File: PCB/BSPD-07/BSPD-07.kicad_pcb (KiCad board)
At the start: 2 copper layers, 78.7 x 30 mm, 17 parts, among them IC1 LM393LVQDRQ1, IC2 LM393LVQDRQ1, IC3 LM393LVQDRQ1, J1 DTM13-12PA

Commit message: New revision with LDO40L
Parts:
- added C1: 0.1uF, Capacitor_SMD:C_0402_1005Metric, F.Cu at (66.7, 72.6)
- added C2: 0.1uF, Capacitor_SMD:C_0402_1005Metric, F.Cu at (66.7, 74.5)
- added C3: 10u, Capacitor_SMD:C_0805_2012Metric, F.Cu at (64.2, 66.1)
- added C4: 0.1uF, Capacitor_SMD:C_0402_1005Metric, F.Cu at (69.6, 72.6)
- added C5: 10uF, Capacitor_SMD:C_0805_2012Metric, F.Cu at (75.6, 66.6)
- added C6: 1uF, Capacitor_SMD:C_0805_2012Metric, F.Cu at (71.2, 66.6)
- added C7: 4.7uF, Capacitor_SMD:C_0805_2012Metric, F.Cu at (71.2, 69.6)
- added IC4: LDO40LPU50RY, BSPD_07:SON95P300X300X90-7N-D, F.Cu at (63.1, 81.9)
- added Q1: RSQ025P03HZGTR, BSPD_07:SOT95P280X100-6N, F.Cu at (68.3, 81.8)
- moved R8 3.34 mm to (54.5, 77.9)
- moved R9 3.34 mm to (51.6, 77.9)
- moved IC1 3.34 mm to (53.0, 63.4)
- moved IC2 3.34 mm to (44.5, 63.4)
- moved IC3 3.34 mm to (45.9, 76.2)
- moved R1 3.34 mm to (51.9, 79.9)
- moved R10 3.34 mm to (54.5, 73.9)
- moved R11 3.34 mm to (51.6, 73.9)
- moved R12 3.34 mm to (51.6, 75.9)
- moved R13 3.34 mm to (57.4, 75.9)
- moved R2 3.34 mm to (48.9, 80.5)
- moved R3 3.34 mm to (51.9, 81.9)
- moved R4 3.34 mm to (57.4, 73.9)
- moved R5 3.34 mm to (46.0, 80.5)
- moved R6 3.34 mm to (43.1, 80.5)
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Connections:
- net ERROR_CUR renamed ERR_CURRENT
- IC1 pad 3: Net-(IC1-Pad3) -> TPS_TRIG
- IC2 pad 3: Net-(IC2-Pad3) -> BRAKE_TRIG
- IC3 pad 1: unconnected-(IC3-Pad1) -> Net-(IC3-Pad1)
- IC3 pad 6: unconnected-(IC3-Pad6) -> Net-(IC3-Pad6)
- J1 pad 7: unconnected-(J1-Pad7) -> BRAKE_TRIG
- J1 pad 8: unconnected-(J1-Pad8) -> TPS_TRIG
- R3 pad 2: Net-(IC1-Pad3) -> TPS_TRIG
- R5 pad 2: Net-(IC2-Pad3) -> BRAKE_TRIG
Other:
- board outline removed

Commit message: Almost finished schematics
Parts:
- added IC5: 74LVC1G02GW-Q100H, BSPD_07:SOT65P212X110-5N, F.Cu at (61.4, 59.8)
- moved IC1 3.68 mm to (52.5, 67.0)
- moved IC2 3.68 mm to (44.0, 67.0)
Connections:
- C6 pad 1: Net-(IC4-Pad2) -> +12V
- J1 pad 5: unconnected-(J1-Pad5) -> SAFETY_IN
- J1 pad 6: unconnected-(J1-Pad6) -> SAFETY_OUT
- J1 pad 7: BRAKE_TRIG -> TPS_TRIG
- J1 pad 8: TPS_TRIG -> BRAKE_TRIG
- J1 pad MH1: unconnected-(J1-PadMH1) -> GND
- J1 pad MH2: unconnected-(J1-PadMH2) -> +12V
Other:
- board outline added: 68.9 x 29.7 mm

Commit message: Finished schematics
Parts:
- added JP1: Jumper_2_Open, Connector_PinHeader_2.54mm:PinHeader_1x02_P2.54mm_Vertical, F.Cu at (75.7, 22.1)
- added Q2: RJU002N06FRAT106, BSPD_07:SOT65P210X100-3N, F.Cu at (82.4, 25.4)
- added R14: 5, Resistor_SMD:R_0402_1005Metric, F.Cu at (85.2, 23.3)
- added R15: 560k, Resistor_SMD:R_0402_1005Metric, F.Cu at (87.2, 23.6)
- added RV1: 20k, BSPD_07:POT-3296X1223LF, F.Cu at (79.7, 36.9)
- added RV2: 20k, BSPD_07:POT-3296X1223LF, F.Cu at (79.7, 45.5)
- added U1: TLP222A, Package_SO:SOP-4_3.8x4.1mm_P2.54mm, F.Cu at (43.2, 32.6)
- added U2: TLP175A, Package_SO:MFSOP6-4_4.4x3.6mm_P1.27mm, F.Cu at (34.4, 32.4)
- IC1, IC2, IC3: footprint PDM_Additional:SOIC127P600X175-8N -> BSPD_07:SOIC127P600X175-8N
- R7, R8: value 100k -> 200k
- moved R3 74.4 mm to (74.4, 11.0), turned to 90 degrees
- moved R6 68.7 mm to (91.6, 31.7), turned to 90 degrees
- moved R5 68.6 mm to (81.6, 21.8), turned to 90 degrees
- moved R2 66.2 mm to (87.2, 26.5), turned to 90 degrees
- moved R9 65.7 mm to (79.4, 18.4), turned to 90 degrees
- moved R1 64.7 mm to (91.6, 28.8), turned to 90 degrees
- moved R10 63.2 mm to (74.4, 13.9), turned to 90 degrees
- moved R4 62.9 mm to (76.4, 13.9), turned to 90 degrees
- moved R8 62.0 mm to (89.2, 26.5), turned to 90 degrees
- moved R13 61.9 mm to (81.6, 18.8), turned to 90 degrees
- moved R11 61.2 mm to (77.4, 18.4), turned to 90 degrees
- moved R12 60.0 mm to (85.2, 26.2), turned to 90 degrees
- moved R7 59.6 mm to (93.6, 30.9), turned to 90 degrees
- moved C1 58.3 mm to (78.4, 15.5), turned to 90 degrees
- moved IC3 58.2 mm to (89.3, 37.4), turned to 90 degrees
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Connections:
- IC3 pad 7: unconnected-(IC3-Pad7) -> Net-(IC3-Pad7)
- IC4 pad 2: Net-(IC4-Pad2) -> +12V
- IC4 pad 3: Net-(IC4-Pad2) -> +12V
- J1 pad 1: unconnected-(J1-Pad1) -> +12V
- J1 pad 11: unconnected-(J1-Pad11) -> BRAKE_IN
- J1 pad 12: unconnected-(J1-Pad12) -> TPS_IN
- J1 pad 2: unconnected-(J1-Pad2) -> GND
- J1 pad MH1: GND -> unconnected-(J1-PadMH1)
- J1 pad MH2: +12V -> unconnected-(J1-PadMH2)
- Q1 pad 3: Net-(IC3-Pad1) -> Net-(Q1-Pad3)
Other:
- board outline removed

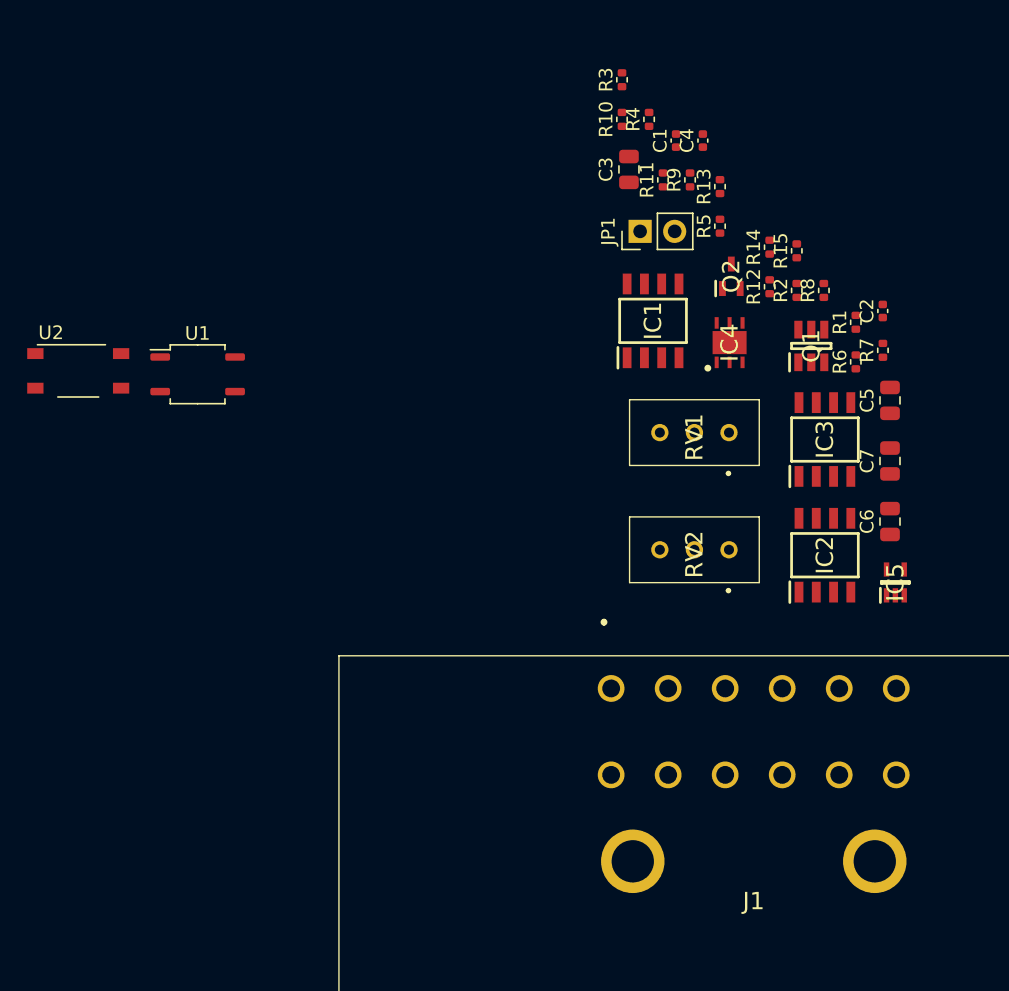
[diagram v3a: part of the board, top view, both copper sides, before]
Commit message: Added info led
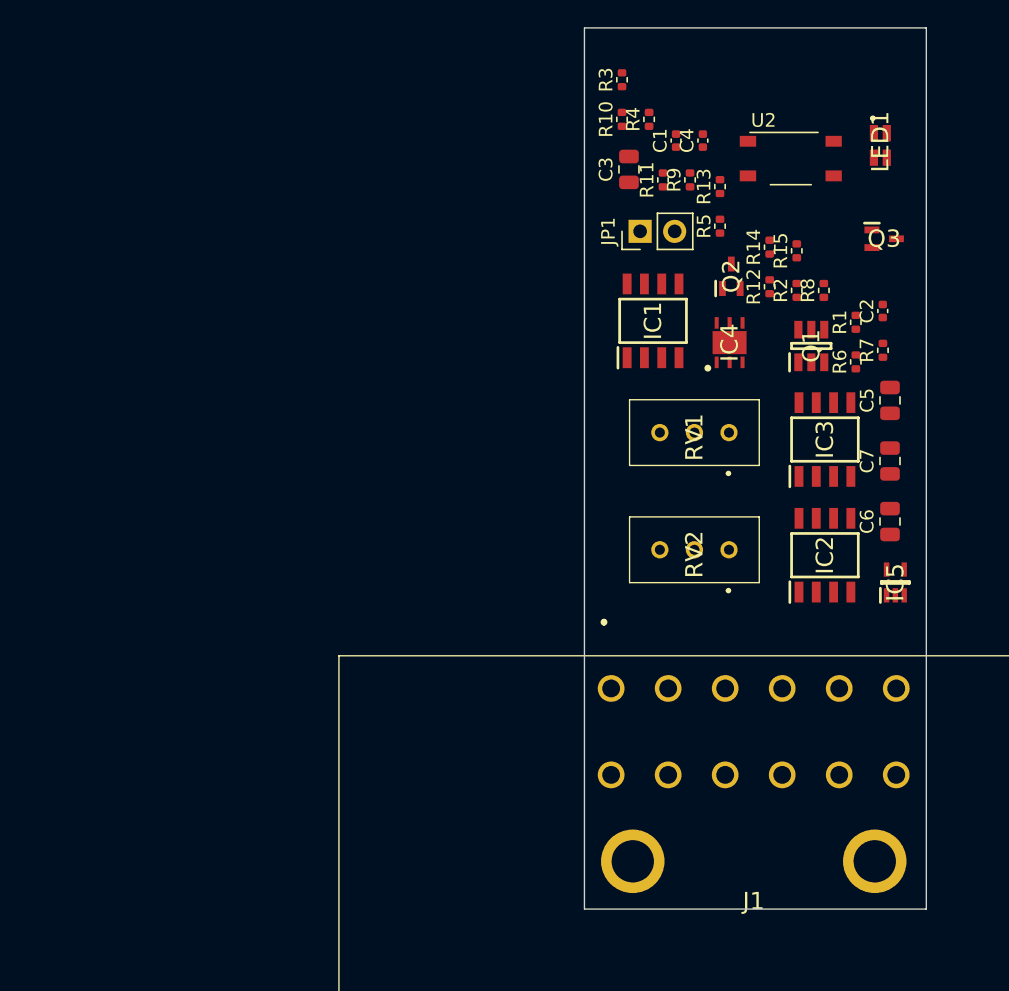
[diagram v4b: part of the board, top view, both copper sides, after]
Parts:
- removed U1: TLP222A, Package_SO:SOP-4_3.8x4.1mm_P2.54mm
- added LED1: APHBM2012SURKCGKC, BSPD_07:APHBM2012SURKCGKC, F.Cu at (93.4, 15.8)
- added Q3: RJU002N06FRAT106, BSPD_07:SOT65P210X100-3N, F.Cu at (93.6, 22.7)
- U2: value TLP175A -> TLP175A / COMUS AB38-Q
- moved U2 54.6 mm to (86.8, 16.8)
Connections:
- U2 pad 1: unconnected-(U2-Pad1) -> Net-(U2-Pad1)
- U2 pad 3: unconnected-(U2-Pad3) -> INFO_LED
- U2 pad 4: unconnected-(U2-Pad4) -> SAFETY_OUT
- U2 pad 6: unconnected-(U2-Pad6) -> SAFETY_IN
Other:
- board outline added: 25.1 x 64.7 mm

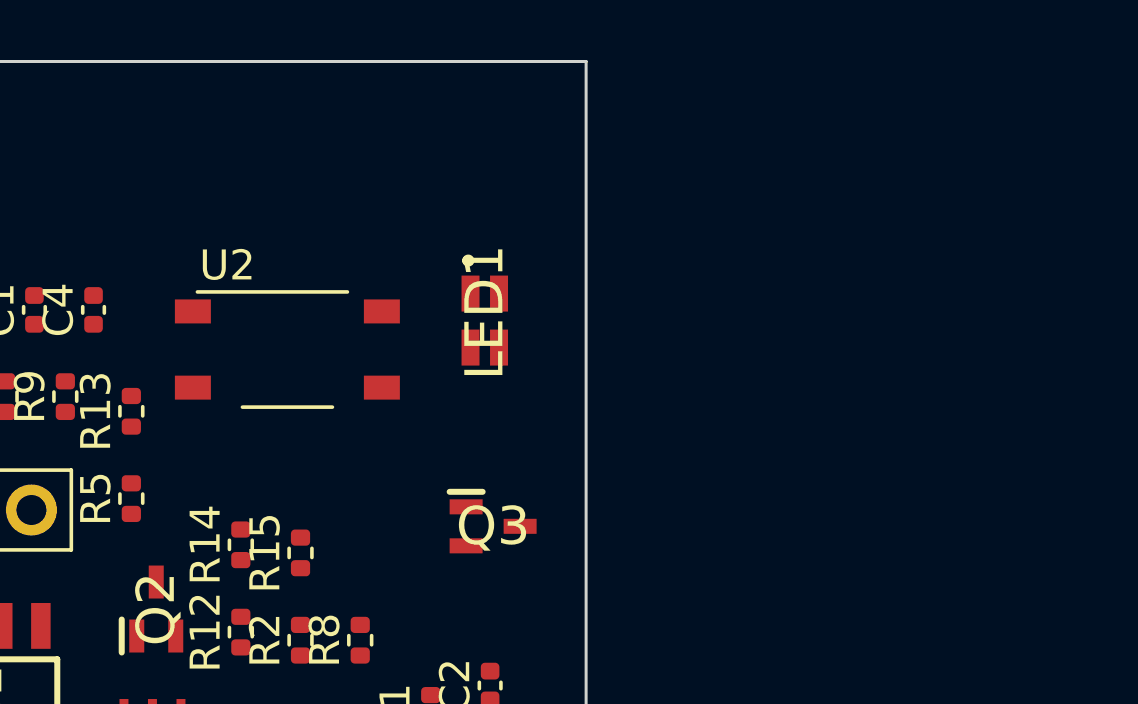
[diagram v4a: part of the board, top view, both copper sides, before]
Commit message: Fixed delay resistor reference value
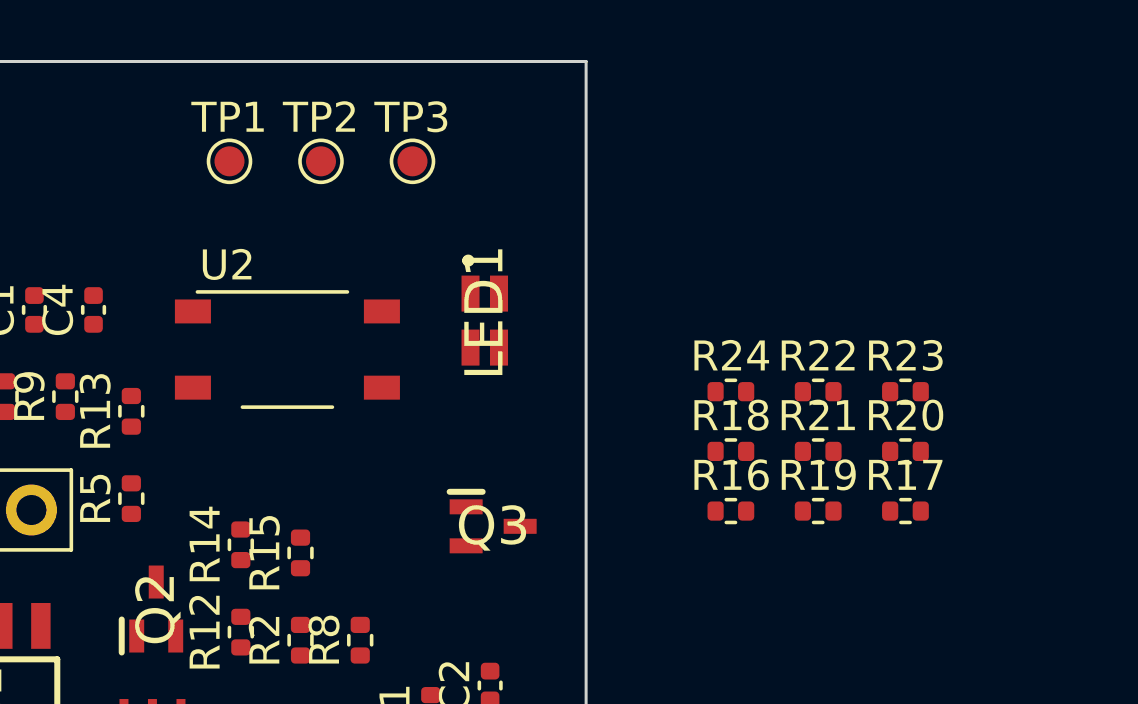
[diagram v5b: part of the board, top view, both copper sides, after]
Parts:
- added R16: 100, Resistor_SMD:R_0402_1005Metric, F.Cu at (101.6, 22.2)
- added R17: 10k, Resistor_SMD:R_0402_1005Metric, F.Cu at (107.4, 22.2)
- added R18: 100, Resistor_SMD:R_0402_1005Metric, F.Cu at (101.6, 20.2)
- added R19: 10k, Resistor_SMD:R_0402_1005Metric, F.Cu at (104.5, 22.2)
- added R20: 560k, Resistor_SMD:R_0402_1005Metric, F.Cu at (107.4, 20.2)
- added R21: 2-4, Resistor_SMD:R_0402_1005Metric, F.Cu at (104.5, 20.2)
- added R22: 1k, Resistor_SMD:R_0402_1005Metric, F.Cu at (104.5, 18.2)
- added R23: 152, Resistor_SMD:R_0402_1005Metric, F.Cu at (107.4, 18.2)
- added R24: 145, Resistor_SMD:R_0402_1005Metric, F.Cu at (101.6, 18.2)
- added TP1: TPS, TestPoint:TestPoint_Pad_D1.0mm, F.Cu at (84.9, 10.5)
- added TP2: BRK, TestPoint:TestPoint_Pad_D1.0mm, F.Cu at (87.9, 10.5)
- added TP3: ERR_FINAL, TestPoint:TestPoint_Pad_D1.0mm, F.Cu at (91.0, 10.5)

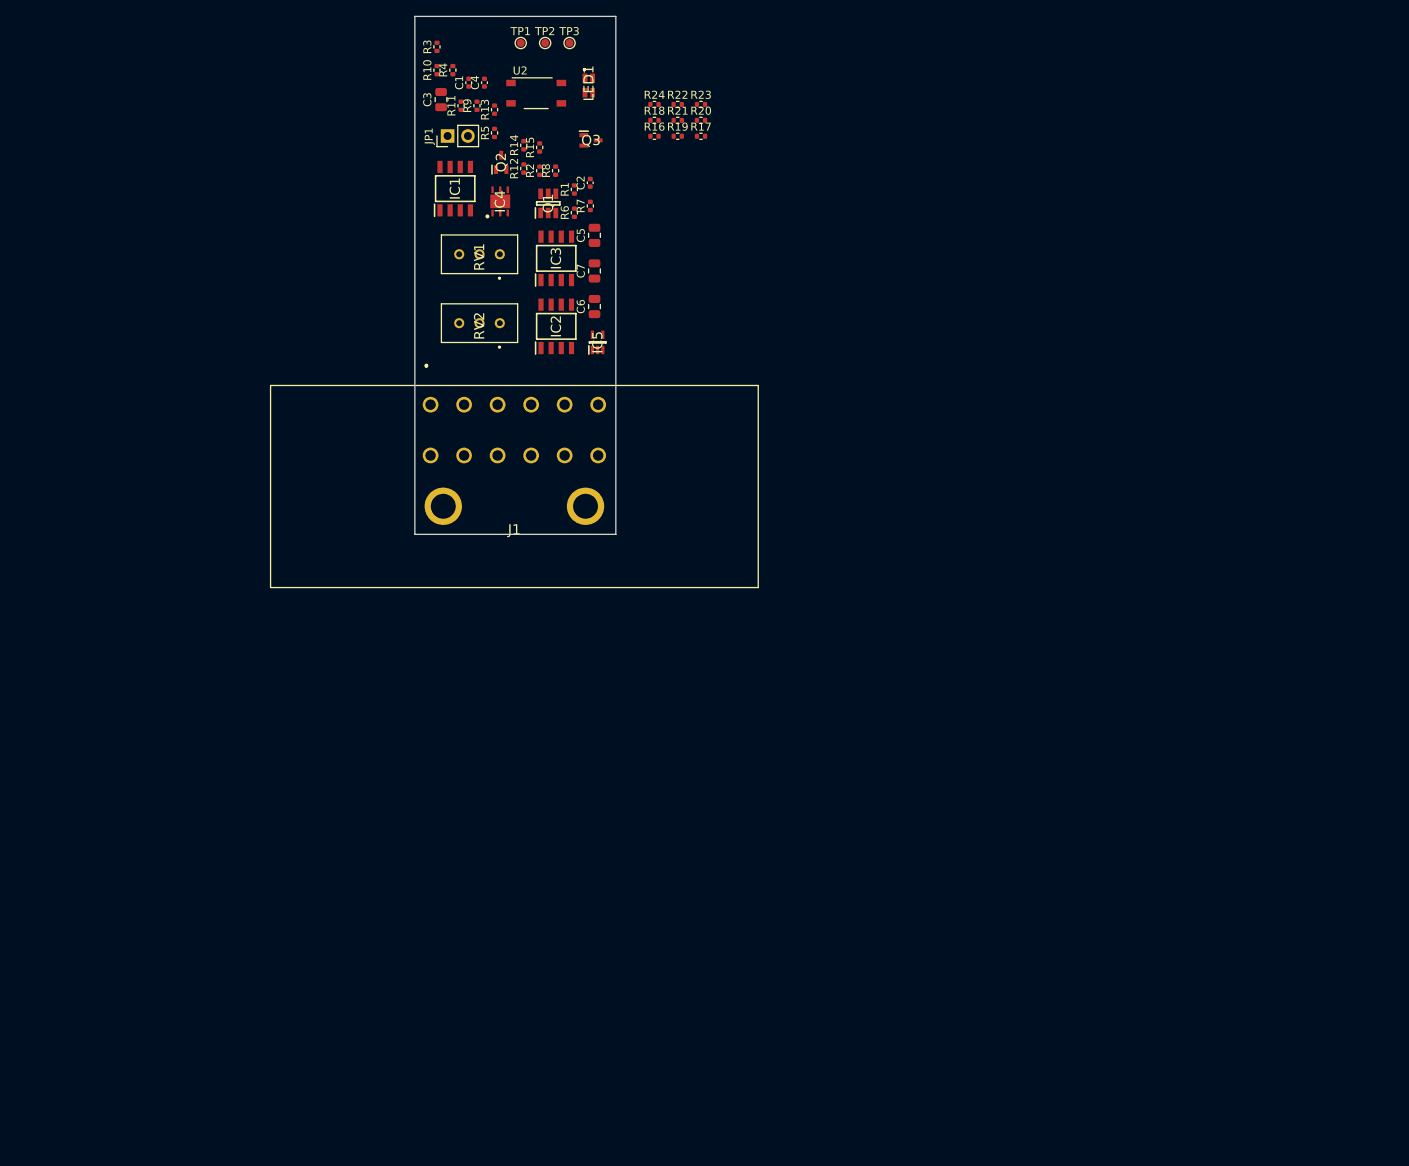
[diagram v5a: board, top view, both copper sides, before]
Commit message: Initial board layout with two comparators
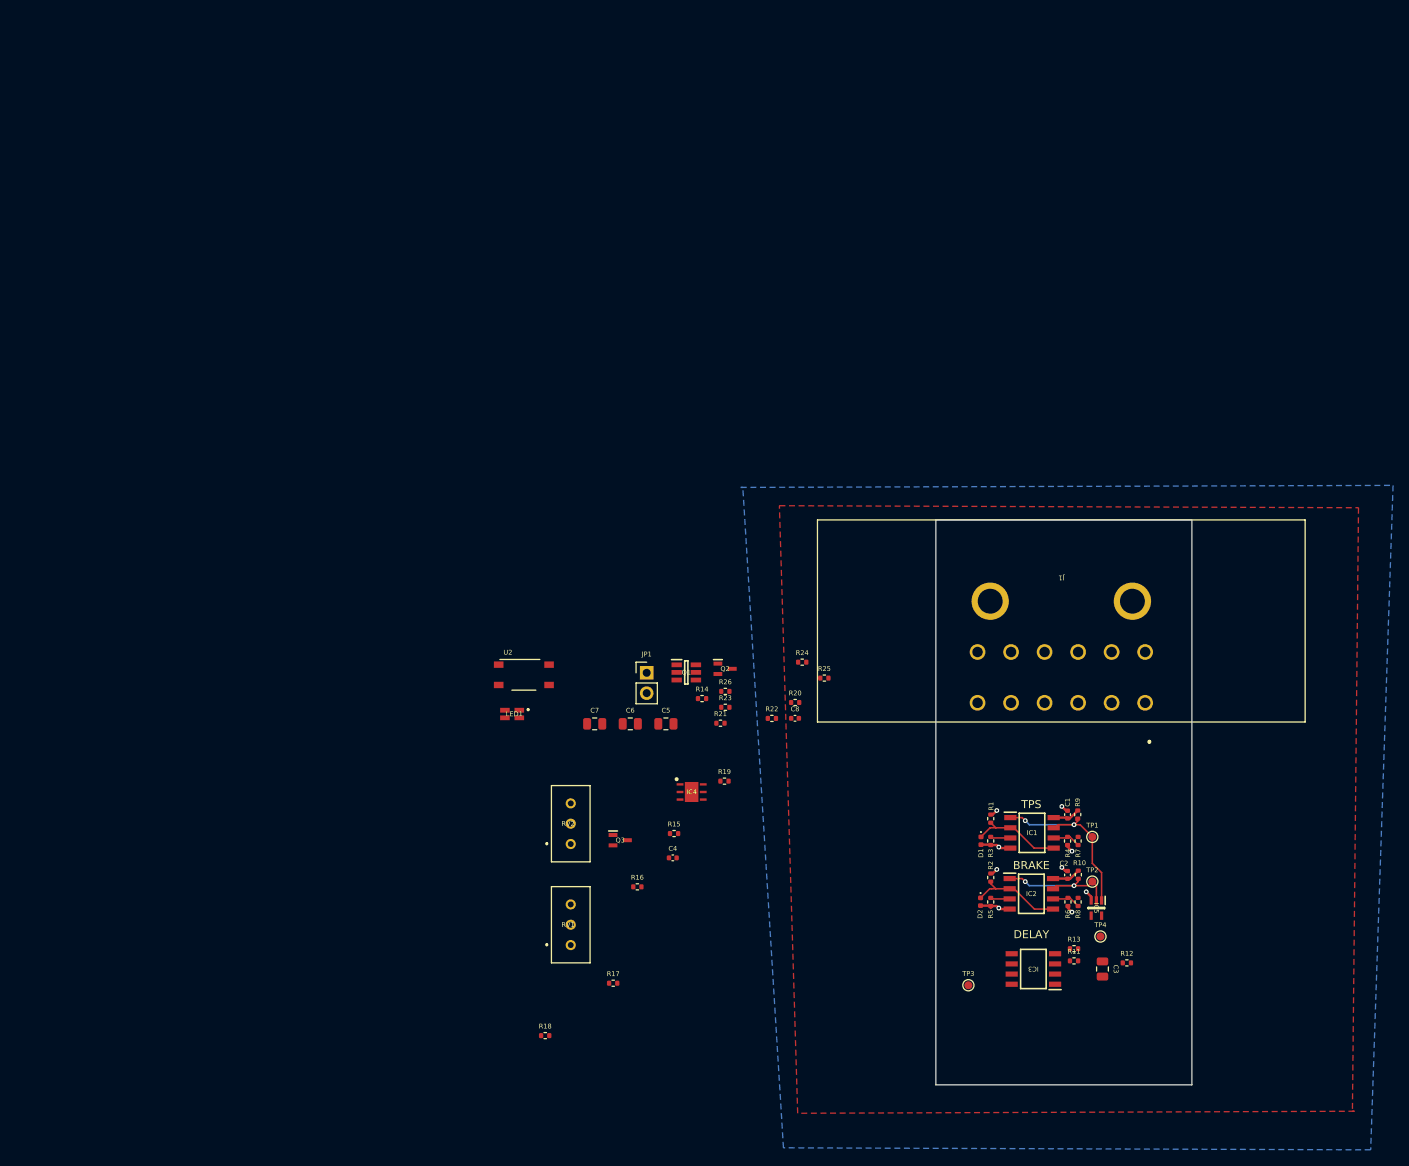
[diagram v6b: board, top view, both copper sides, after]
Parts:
- added C8: 0.1u, Capacitor_SMD:C_0402_1005Metric, F.Cu at (119.1, 94.9)
- added D1: 7V, Diode_SMD:D_0402_1005Metric, F.Cu at (142.4, 110.2)
- added D2: 7V, Diode_SMD:D_0402_1005Metric, F.Cu at (142.3, 117.9)
- added R25: 39k, Resistor_SMD:R_0402_1005Metric, F.Cu at (122.8, 89.9)
- added R26: 10k, Resistor_SMD:R_0402_1005Metric, F.Cu at (110.4, 91.6)
- added TP4: CUR, TestPoint:TestPoint_Pad_D1.0mm, F.Cu at (157.3, 122.2)
- moved C3 136.6 mm to (157.6, 126.3), turned to -90 degrees
- moved R11 131.5 mm to (154.0, 125.2), turned to 0 degrees
- moved R10 128.6 mm to (154.6, 114.5)
- moved TP3 127.9 mm to (140.8, 128.3)
- moved R13 127.5 mm to (154.0, 123.7), turned to 0 degrees
- moved TP2 125.2 mm to (156.3, 115.3)
- moved R12 124.7 mm to (160.6, 125.5), turned to 0 degrees
- moved R4 123.2 mm to (153.2, 110.3)
- moved TP1 122.3 mm to (156.3, 109.8)
- moved R3 121.0 mm to (143.6, 110.3)
- moved C1 118.2 mm to (153.2, 107.0), turned to -90 degrees
- moved R9 116.1 mm to (154.5, 107.0)
- moved R18 115.2 mm to (87.9, 134.6)
- moved R5 114.4 mm to (143.6, 117.9)
- moved R8 112.3 mm to (154.5, 117.9)
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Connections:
- IC3 pad 5: unconnected-(IC3-Pad5) -> Net-(IC3-Pad5)
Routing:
- net TPS_COMP_OUT: track 0.00 -> 23.6 mm, vias 0 -> 2
- net BRAKE_COMP_OUT: track 0.00 -> 17.3 mm, vias 0 -> 2
- net GND: track 0.00 -> 15.1 mm, vias 0 -> 9
- net BRAKE_IN: track 0.00 -> 11.7 mm
- net TPS_IN: track 0.00 -> 11.7 mm
- net +5V: track 0.00 -> 7.04 mm
- net Net-(IC1-Pad6): track 0.00 -> 3.70 mm
- net Net-(IC2-Pad6): track 0.00 -> 3.61 mm
- net TPS_TRIG: track 0.00 -> 2.71 mm
- net BRAKE_TRIG: track 0.00 -> 2.42 mm
- added copper zone on F.Cu, net +5V
- added copper zone on B.Cu, net GND
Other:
- board size 25.1 x 64.7 mm -> 32 x 70.6 mm
- board text added: "BRAKE"
- board text added: "DELAY"
- board text added: "TPS"
